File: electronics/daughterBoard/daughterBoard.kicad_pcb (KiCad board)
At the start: 2 copper layers, 28 x 53 mm, 10 parts, among them P1 CONN_01X02, P2 CONN_01X04, Q1 BSS138, U1 MAX98357A, U2 RaspberryPI_zero_GPIO

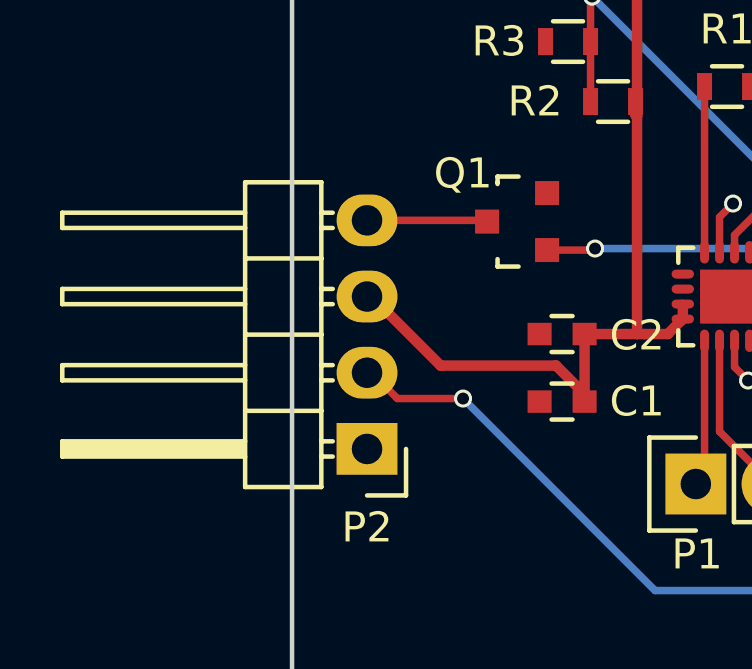
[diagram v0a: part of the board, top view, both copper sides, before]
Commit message: Added daughterboard PCB
Added V1 of the pcb with sound support. Not tested yet, boards are
still on their way from Shenzen2u.
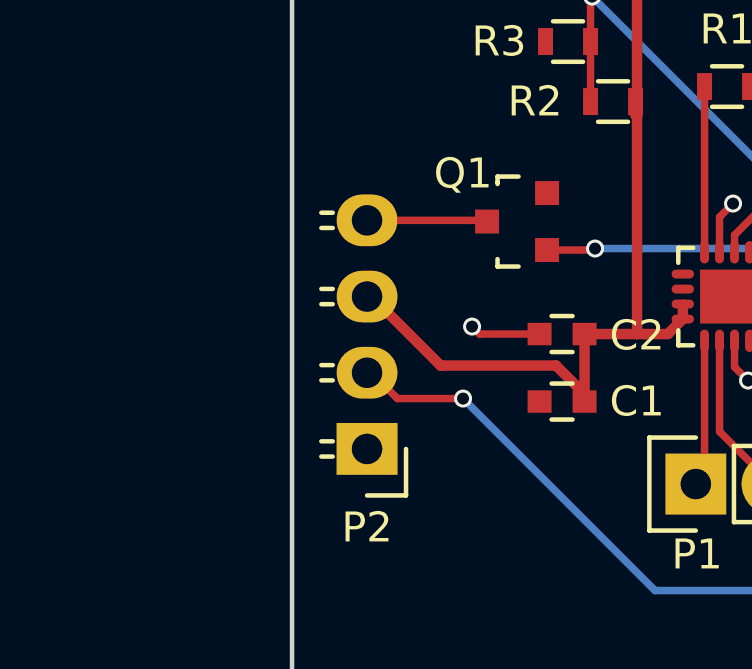
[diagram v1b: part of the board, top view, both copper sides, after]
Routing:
- net GND: track 4.61 -> 6.96 mm, vias 3 -> 4
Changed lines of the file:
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@@
     (links 35)
     (no_connects 2)
-    (area 156.924999 97.924999 185.075001 151.075001)
+    (area 148.624999 87.5 201.85 151.075001)
     (thickness 1.6)
     (drawings 7)
-    (tracks 77)
+    (tracks 80)
     (zones 0)
     (modules 10)
@@
     (visible_elements FFFFFF7F)
     (pcbplotparams
-      (layerselection 0x00030_80000001)
+      (layerselection 0x010fc_80000001)
       (usegerberextensions false)
       (excludeedgelayer true)
@@
     (add_net +5V)
   )
+  (module Pin_Headers:Pin_Header_Angled_1x04 (layer F.Cu)
+    (at 159.5 132.58 180)
+    (descr "Through hole pin header")
+    (tags "pin header")
+    (attr virtual)
+    (fp_text reference P2 (at 0 -2.62 180) (layer F.SilkS)
+      (effects (font (size 1 1) (thickness 0.15)))
+    )
+    (fp_text value CONN_01X04 (at 0 -3.1 180) (layer F.Fab)
+      (effects (font (size 1 1) (thickness 0.15)))
+    )
+    (fp_line (start -1.5 -1.75) (end -1.5 9.4) (layer F.CrtYd) (width 0.05))
+    (fp_line (start 10.65 -1.75) (end 10.65 9.4) (layer F.CrtYd) (width 0.05))
+    (fp_line (start -1.5 -1.75) (end 10.65 -1.75) (layer F.CrtYd) (width 0.05))
+    (fp_line (start -1.5 9.4) (end 10.65 9.4) (layer F.CrtYd) (width 0.05))
+    (fp_line (start -1.3 -1.55) (end -1.3 0) (layer F.SilkS) (width 0.15))
+    (fp_line (start 0 -1.55) (end -1.3 -1.55) (layer F.SilkS) (width 0.15))
+    (fp_line (start 1.524 -0.254) (end 1.143 -0.254) (layer F.SilkS) (width 0.15))
+    (fp_line (start 1.524 0.254) (end 1.143 0.254) (layer F.SilkS) (width 0.15))
+    (fp_line (start 1.524 2.286) (end 1.143 2.286) (layer F.SilkS) (width 0.15))
+    (fp_line (start 1.524 2.794) (end 1.143 2.794) (layer F.SilkS) (width 0.15))
+    (fp_line (start 1.524 4.826) (end 1.143 4.826) (layer F.SilkS) (width 0.15))
+    (fp_line (start 1.524 5.334) (end 1.143 5.334) (layer F.SilkS) (width 0.15))
+    (fp_line (start 1.524 7.874) (end 1.143 7.874) (layer F.SilkS) (width 0.15))
+    (fp_line (start 1.524 7.366) (end 1.143 7.366) (layer F.SilkS) (width 0.15))
+    (pad 1 thru_hole rect (at 0 0 180) (size 2.032 1.7272) (drill 1.016) (layers *.Cu *.Mask F.SilkS)
+      (net 1 GND))
+    (pad 2 thru_hole oval (at 0 2.54 180) (size 2.032 1.7272) (drill 1.016) (layers *.Cu *.Mask F.SilkS)
+      (net 5 BTN))
+    (pad 3 thru_hole oval (at 0 5.08 180) (size 2.032 1.7272) (drill 1.016) (layers *.Cu *.Mask F.SilkS)
+      (net 2 +5V))
+    (pad 4 thru_hole oval (at 0 7.62 180) (size 2.032 1.7272) (drill 1.016) (layers *.Cu *.Mask F.SilkS)
+      (net 12 "Net-(P2-Pad4)"))
+    (model Pin_Headers.3dshapes/Pin_Header_Angled_1x04.wrl
+      (at (xyz 0 -0.15 0))
+      (scale (xyz 1 1 1))
+      (rotate (xyz 0 0 90))
+    )
+  )
   (module Capacitors_SMD:C_0603 (layer F.Cu)
     (at 166 131)
@@
     )
   )
-  (module Pin_Headers:Pin_Header_Angled_1x04 (layer F.Cu)
-    (at 159.5 132.58 180)
-    (descr "Through hole pin header")
-    (tags "pin header")
-    (fp_text reference P2 (at 0 -2.62 180) (layer F.SilkS)
-      (effects (font (size 1 1) (thickness 0.15)))
-    )
-    (fp_text value CONN_01X04 (at 0 -3.1 180) (layer F.Fab)
-      (effects (font (size 1 1) (thickness 0.15)))
-    )
-    (fp_line (start -1.5 -1.75) (end -1.5 9.4) (layer F.CrtYd) (width 0.05))
-    (fp_line (start 10.65 -1.75) (end 10.65 9.4) (layer F.CrtYd) (width 0.05))
-    (fp_line (start -1.5 -1.75) (end 10.65 -1.75) (layer F.CrtYd) (width 0.05))
-    (fp_line (start -1.5 9.4) (end 10.65 9.4) (layer F.CrtYd) (width 0.05))
-    (fp_line (start -1.3 -1.55) (end -1.3 0) (layer F.SilkS) (width 0.15))
-    (fp_line (start 0 -1.55) (end -1.3 -1.55) (layer F.SilkS) (width 0.15))
-    (fp_line (start 4.191 -0.127) (end 10.033 -0.127) (layer F.SilkS) (width 0.15))
-    (fp_line (start 10.033 -0.127) (end 10.033 0.127) (layer F.SilkS) (width 0.15))
-    (fp_line (start 10.033 0.127) (end 4.191 0.127) (layer F.SilkS) (width 0.15))
-    (fp_line (start 4.191 0.127) (end 4.191 0) (layer F.SilkS) (width 0.15))
-    (fp_line (start 4.191 0) (end 10.033 0) (layer F.SilkS) (width 0.15))
-    (fp_line (start 1.524 -0.254) (end 1.143 -0.254) (layer F.SilkS) (width 0.15))
-    (fp_line (start 1.524 0.254) (end 1.143 0.254) (layer F.SilkS) (width 0.15))
-    (fp_line (start 1.524 2.286) (end 1.143 2.286) (layer F.SilkS) (width 0.15))
-    (fp_line (start 1.524 2.794) (end 1.143 2.794) (layer F.SilkS) (width 0.15))
-    (fp_line (start 1.524 4.826) (end 1.143 4.826) (layer F.SilkS) (width 0.15))
-    (fp_line (start 1.524 5.334) (end 1.143 5.334) (layer F.SilkS) (width 0.15))
-    (fp_line (start 1.524 7.874) (end 1.143 7.874) (layer F.SilkS) (width 0.15))
-    (fp_line (start 1.524 7.366) (end 1.143 7.366) (layer F.SilkS) (width 0.15))
-    (fp_line (start 1.524 -1.27) (end 4.064 -1.27) (layer F.SilkS) (width 0.15))
-    (fp_line (start 1.524 1.27) (end 4.064 1.27) (layer F.SilkS) (width 0.15))
-    (fp_line (start 1.524 1.27) (end 1.524 3.81) (layer F.SilkS) (width 0.15))
-    (fp_line (start 1.524 3.81) (end 4.064 3.81) (layer F.SilkS) (width 0.15))
-    (fp_line (start 4.064 2.286) (end 10.16 2.286) (layer F.SilkS) (width 0.15))
-    (fp_line (start 10.16 2.286) (end 10.16 2.794) (layer F.SilkS) (width 0.15))
-    (fp_line (start 10.16 2.794) (end 4.064 2.794) (layer F.SilkS) (width 0.15))
-    (fp_line (start 4.064 3.81) (end 4.064 1.27) (layer F.SilkS) (width 0.15))
-    (fp_line (start 4.064 1.27) (end 4.064 -1.27) (layer F.SilkS) (width 0.15))
-    (fp_line (start 10.16 0.254) (end 4.064 0.254) (layer F.SilkS) (width 0.15))
-    (fp_line (start 10.16 -0.254) (end 10.16 0.254) (layer F.SilkS) (width 0.15))
-    (fp_line (start 4.064 -0.254) (end 10.16 -0.254) (layer F.SilkS) (width 0.15))
-    (fp_line (start 1.524 1.27) (end 4.064 1.27) (layer F.SilkS) (width 0.15))
-    (fp_line (start 1.524 -1.27) (end 1.524 1.27) (layer F.SilkS) (width 0.15))
-    (fp_line (start 1.524 6.35) (end 4.064 6.35) (layer F.SilkS) (width 0.15))
-    (fp_line (start 1.524 6.35) (end 1.524 8.89) (layer F.SilkS) (width 0.15))
-    (fp_line (start 1.524 8.89) (end 4.064 8.89) (layer F.SilkS) (width 0.15))
-    (fp_line (start 4.064 7.366) (end 10.16 7.366) (layer F.SilkS) (width 0.15))
-    (fp_line (start 10.16 7.366) (end 10.16 7.874) (layer F.SilkS) (width 0.15))
-    (fp_line (start 10.16 7.874) (end 4.064 7.874) (layer F.SilkS) (width 0.15))
-    (fp_line (start 4.064 8.89) (end 4.064 6.35) (layer F.SilkS) (width 0.15))
-    (fp_line (start 4.064 6.35) (end 4.064 3.81) (layer F.SilkS) (width 0.15))
-    (fp_line (start 10.16 5.334) (end 4.064 5.334) (layer F.SilkS) (width 0.15))
-    (fp_line (start 10.16 4.826) (end 10.16 5.334) (layer F.SilkS) (width 0.15))
-    (fp_line (start 4.064 4.826) (end 10.16 4.826) (layer F.SilkS) (width 0.15))
-    (fp_line (start 1.524 6.35) (end 4.064 6.35) (layer F.SilkS) (width 0.15))
-    (fp_line (start 1.524 3.81) (end 1.524 6.35) (layer F.SilkS) (width 0.15))
-    (fp_line (start 1.524 3.81) (end 4.064 3.81) (layer F.SilkS) (width 0.15))
-    (pad 1 thru_hole rect (at 0 0 180) (size 2.032 1.7272) (drill 1.016) (layers *.Cu *.Mask F.SilkS)
-      (net 1 GND))
-    (pad 2 thru_hole oval (at 0 2.54 180) (size 2.032 1.7272) (drill 1.016) (layers *.Cu *.Mask F.SilkS)
-      (net 5 BTN))
-    (pad 3 thru_hole oval (at 0 5.08 180) (size 2.032 1.7272) (drill 1.016) (layers *.Cu *.Mask F.SilkS)
-      (net 2 +5V))
-    (pad 4 thru_hole oval (at 0 7.62 180) (size 2.032 1.7272) (drill 1.016) (layers *.Cu *.Mask F.SilkS)
-      (net 12 "Net-(P2-Pad4)"))
-    (model Pin_Headers.3dshapes/Pin_Header_Angled_1x04.wrl
-      (at (xyz 0 -0.15 0))
-      (scale (xyz 1 1 1))
-      (rotate (xyz 0 0 90))
-    )
-  )
   (module TO_SOT_Packages_SMD:SOT-23 (layer F.Cu)
     (at 164.5 125 90)
@@
   (gr_line (start 185 151) (end 157 151) (layer Edge.Cuts) (width 0.15))
   (gr_line (start 185 98) (end 185 151) (layer Edge.Cuts) (width 0.15))
+  (segment (start 163.25 128.75) (end 163 128.5) (width 0.25) (layer F.Cu) (net 1))
+  (segment (start 165.25 128.75) (end 163.25 128.75) (width 0.25) (layer F.Cu) (net 1))
+  (via (at 163 128.5) (size 0.6) (drill 0.4) (layers F.Cu B.Cu) (net 1))
   (segment (start 174.081575 127.25) (end 174.206585 127.12499) (width 0.25) (layer F.Cu) (net 1))
   (segment (start 172.975 127.25) (end 174.081575 127.25) (width 0.25) (layer F.Cu) (net 1))
